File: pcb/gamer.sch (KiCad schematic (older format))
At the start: 38 parts, among them J1 Conn_01x02, J2 Conn_01x04, J3 USB_B_Mini, J4 Conn_01x08, J5 Micro_SD_Card, SW1 SW_DIP_x01, SW2 SW_DIP_x01, SW3 SW_DIP_x01, SW4 SW_DIP_x01, SW5 SW_Push, SW6 SW_SPDT, U1 MIC5205-3.3YM5, U2 STM32F103RBTx, Y1 Crystal

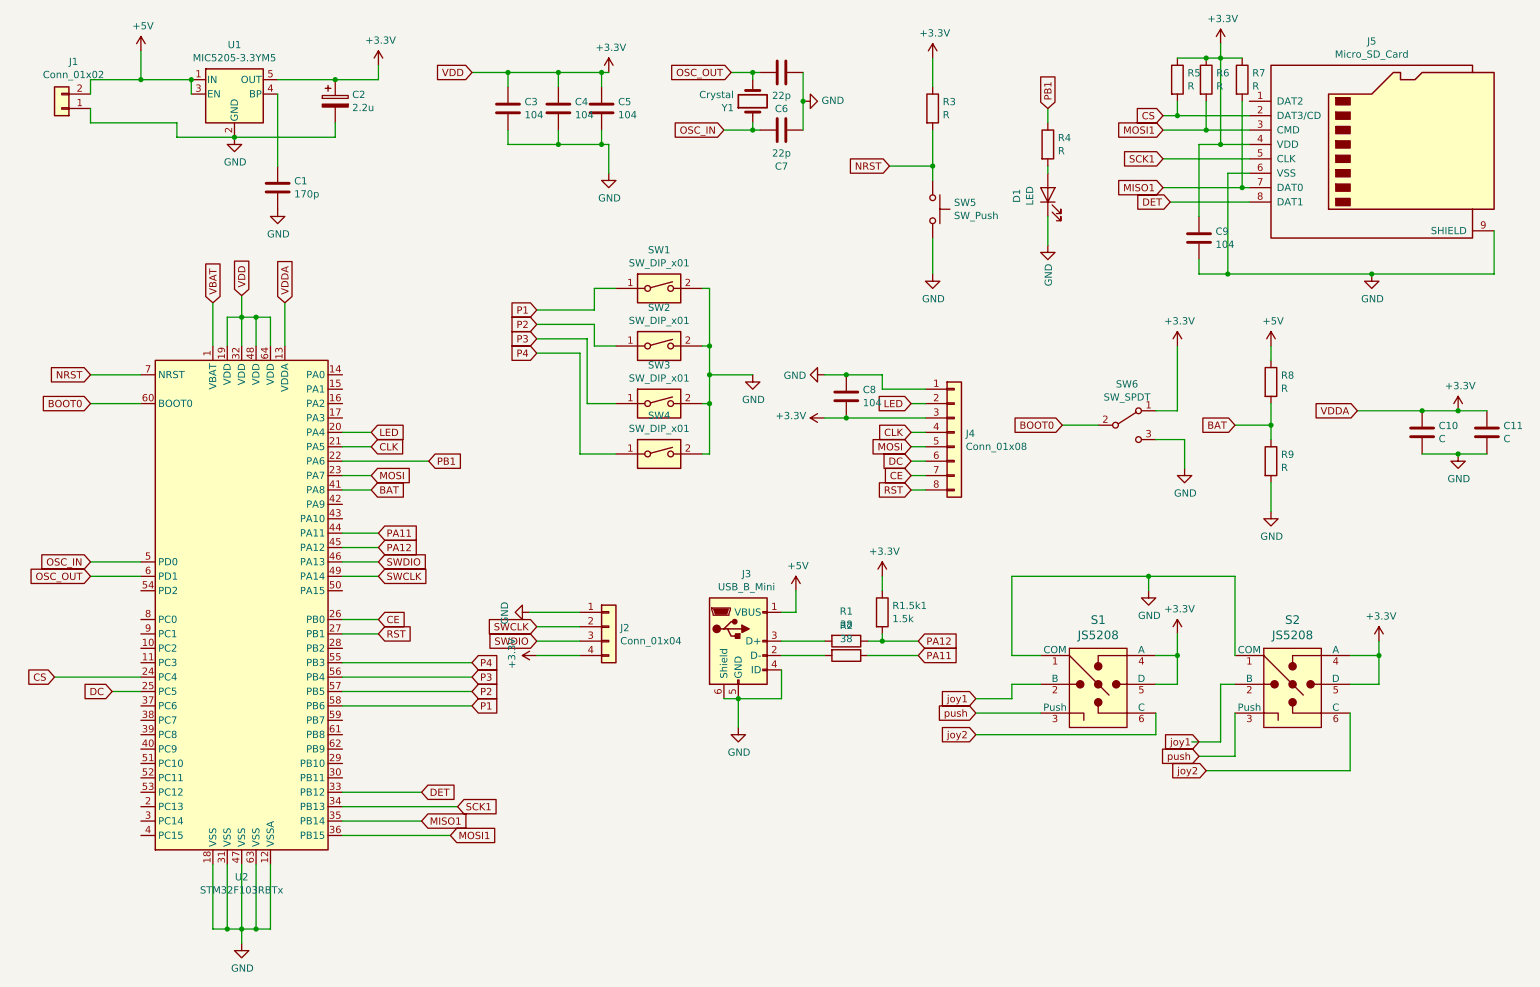
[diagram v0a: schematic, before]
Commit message: update schematic
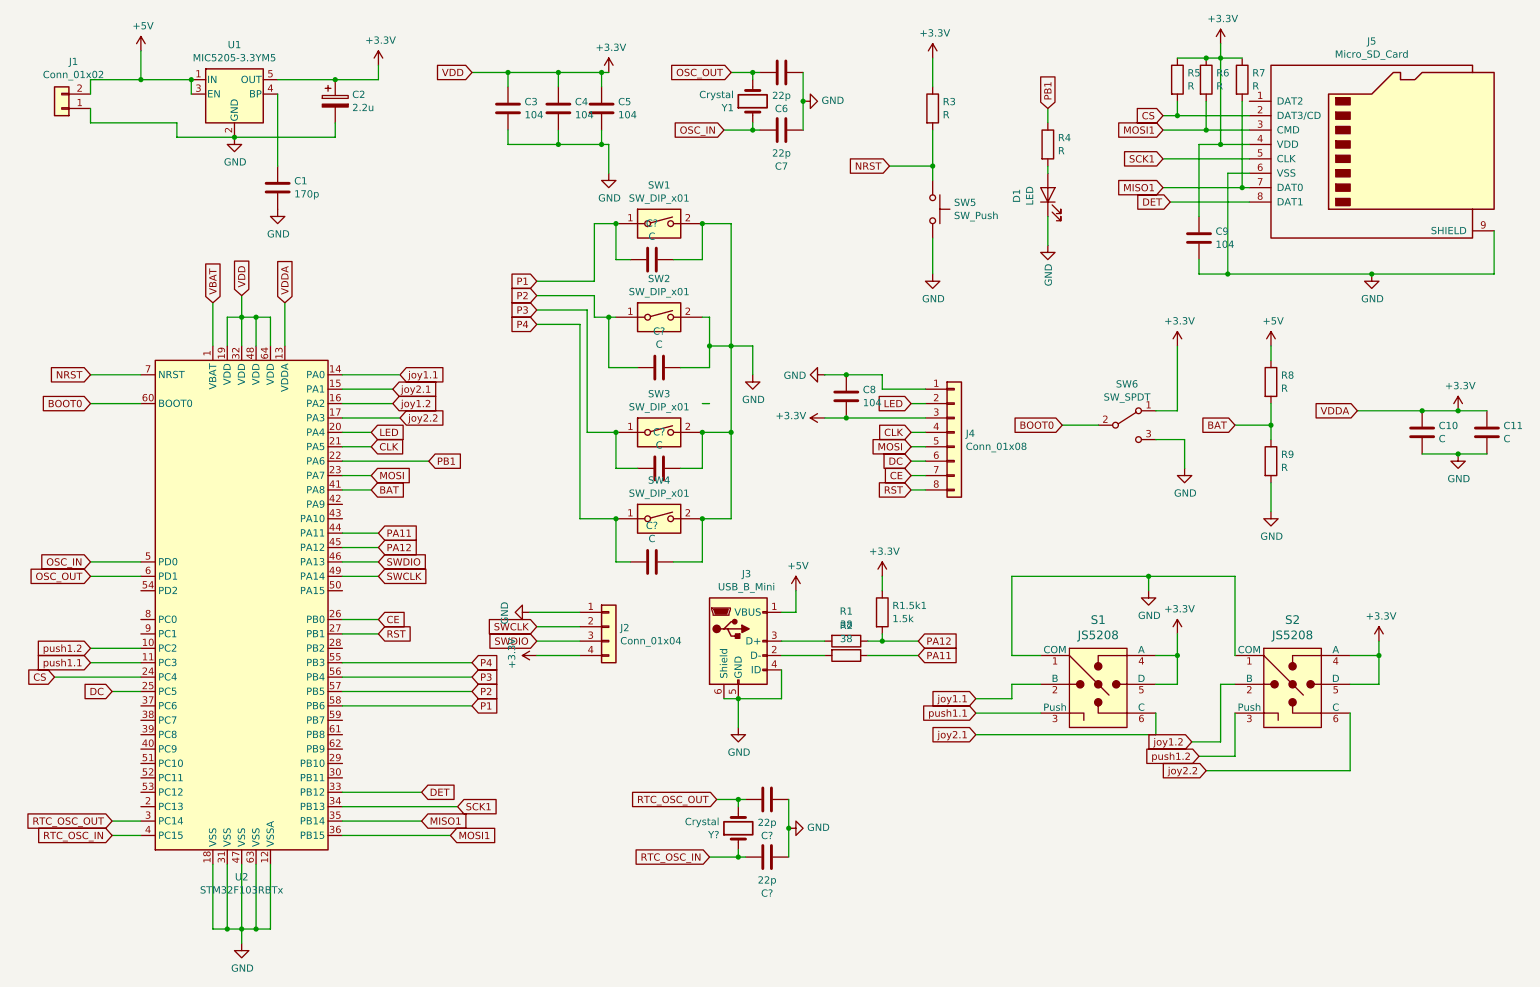
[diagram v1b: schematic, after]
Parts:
- added C? (x4): C, symbol Device:C
- added C? (x2): 22p, Capacitor_SMD:C_0603_1608Metric_Pad1.05x0.95mm_HandSolder, symbol Device:C
- added Y?: Crystal, Crystal:Crystal_SMD_0603-2Pin_6.0x3.5mm, symbol Device:Crystal
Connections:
- net GND: now also C?.1, C?.1, C?.1, C?.1, C?.2, C?.2
- net P1: now also C?.2
- net P2: now also C?.2
- net P3: now also C?.2
- net P4: now also C?.2
- net push1.2: now reaches U2.10 (PC2)
- net push1.2: now also S2.3 (Push)
- net push1.1: now reaches U2.11 (PC3)
- net push1.1: now also S1.3 (Push)
- net joy1.1: now reaches U2.14 (PA0)
- net joy1.1: now also S1.2 (B)
- net joy2.1: now reaches U2.15 (PA1)
- net joy2.1: now also S1.6 (C)
- net joy1.2: now reaches U2.16 (PA2)
- net joy1.2: now also S2.2 (B)
- net joy2.2: now reaches U2.17 (PA3)
- net joy2.2: now also S2.6 (C)
- net RTC_OSC_OUT: now reaches U2.3 (PC14)
- net RTC_OSC_OUT: now also C?.1, Y?.2
- net RTC_OSC_IN: now reaches U2.4 (PC15)
- net RTC_OSC_IN: now also C?.1, Y?.1
- removed net joy1: S1.2 (B), S2.2 (B)
- removed net joy2: S1.6 (C), S2.6 (C)
- removed net push: S1.3 (Push), S2.3 (Push)
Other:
- moved on the sheet: SW1, SW2, SW3, SW4
